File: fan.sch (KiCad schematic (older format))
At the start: 14 parts, among them J7 Fan In, J8 Fan Out, Q1 2N7002, Q2 2N7002, U9 TMP709

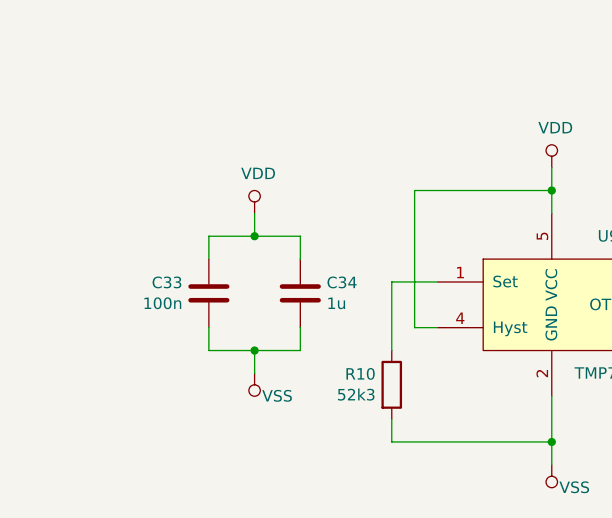
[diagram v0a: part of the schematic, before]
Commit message: Added optional through hole resistor to set fan switch on temperature.
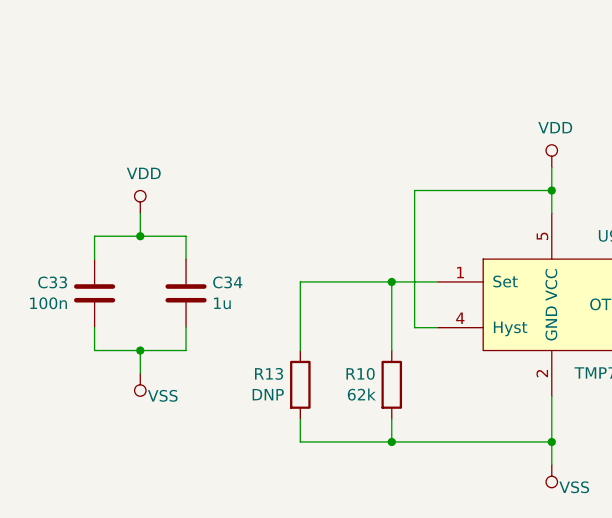
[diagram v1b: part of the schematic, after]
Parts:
- added R13: DNP, Resistor_THT:R_Axial_DIN0207_L6.3mm_D2.5mm_P10.16mm_Horizontal, symbol Device:R
- R10: value 52k3 -> 62k; lcsc# C218068 -> C351636; manf# ARG03FTC5232 -> PTFR0603B62K0P9
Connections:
- net VSS: now also R13.2
- net at R10.1, U9.1 (Set): now also R13.1
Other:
- moved on the sheet: C33, C34
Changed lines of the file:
@@
 AR Path="/5E453957/5E4A10E3" Ref="R10"  Part="1"
 F 0 "R10" H 2630 3896 50  0000 R CNN
-F 1 "52k3" H 2630 3805 50  0000 R CNN
+F 1 "62k" H 2630 3805 50  0000 R CNN
 F 2 "Resistor_SMD:R_0603_1608Metric" V 2630 3850 50  0001 C CNN
 F 3 "~" H 2700 3850 50  0001 C CNN
-F 4 "C218068" H 2700 3850 50  0001 C CNN "lcsc#"
-F 5 "ARG03FTC5232" H 2700 3850 50  0001 C CNN "manf#"
+F 4 "C351636" H 2700 3850 50  0001 C CNN "lcsc#"
+F 5 "PTFR0603B62K0P9" H 2700 3850 50  0001 C CNN "manf#"
 	1    2700 3850
 	1    0    0    -1
@@
 L Device:C C?
 U 1 1 5E4BEA5F
-P 1900 3450
+P 1400 3450
 AR Path="/5DD6D4DA/5DD6D50E/5E4BEA5F" Ref="C?"  Part="1"
 AR Path="/5DD6D4DA/5DDED058/5E4BEA5F" Ref="C?"  Part="1"
@@
 AR Path="/5E4BEA5F" Ref="C?"  Part="1"
 AR Path="/5E453957/5E4BEA5F" Ref="C33"  Part="1"
-F 0 "C33" H 2015 3496 50  0000 L CNN
-F 1 "100n" H 2015 3405 50  0000 L CNN
-F 2 "Capacitor_SMD:C_0603_1608Metric" H 1938 3300 50  0001 C CNN
-F 3 "~" H 1900 3450 50  0001 C CNN
-F 4 "CC0603KRX7R9BB104" H 1900 3450 50  0001 C CNN "manf#"
-F 5 "C14663" H 1900 3450 50  0001 C CNN "lcsc#"
-	1    1900 3450
+F 0 "C33" H 1515 3496 50  0000 L CNN
+F 1 "100n" H 1515 3405 50  0000 L CNN
+F 2 "Capacitor_SMD:C_0603_1608Metric" H 1438 3300 50  0001 C CNN
+F 3 "~" H 1400 3450 50  0001 C CNN
+F 4 "CC0603KRX7R9BB104" H 1400 3450 50  0001 C CNN "manf#"
+F 5 "C14663" H 1400 3450 50  0001 C CNN "lcsc#"
+	1    1400 3450
 	-1   0    0    -1
 $EndComp
@@
 L Device:C C?
 U 1 1 5E4BEA67
-P 2300 3450
+P 1800 3450
 AR Path="/5DD6D4DA/5DD6D50E/5E4BEA67" Ref="C?"  Part="1"
 AR Path="/5DD6D4DA/5DDED058/5E4BEA67" Ref="C?"  Part="1"
@@
 AR Path="/5E4BEA67" Ref="C?"  Part="1"
 AR Path="/5E453957/5E4BEA67" Ref="C34"  Part="1"
-F 0 "C34" H 2415 3496 50  0000 L CNN
-F 1 "1u" H 2415 3405 50  0000 L CNN
-F 2 "Capacitor_SMD:C_0805_2012Metric" H 2338 3300 50  0001 C CNN
-F 3 "~" H 2300 3450 50  0001 C CNN
-F 4 "CL21B105KBFNNNE" H 2300 3450 50  0001 C CNN "manf#"
-F 5 "C28323" H 2300 3450 50  0001 C CNN "lcsc#"
-	1    2300 3450
-	1    0    0    -1
-$EndComp
-Wire Wire Line
-	2100 3200 2100 3100
+F 0 "C34" H 1915 3496 50  0000 L CNN
+F 1 "1u" H 1915 3405 50  0000 L CNN
+F 2 "Capacitor_SMD:C_0805_2012Metric" H 1838 3300 50  0001 C CNN
+F 3 "~" H 1800 3450 50  0001 C CNN
+F 4 "CL21B105KBFNNNE" H 1800 3450 50  0001 C CNN "manf#"
+F 5 "C28323" H 1800 3450 50  0001 C CNN "lcsc#"
+	1    1800 3450
+	1    0    0    -1
+$EndComp
+Wire Wire Line
+	1600 3200 1600 3100
 $Comp
 L power:VDD #PWR?
 U 1 1 5E4C0B54
-P 2100 3100
+P 1600 3100
 AR Path="/5E3D0FD8/5E4C0B54" Ref="#PWR?"  Part="1"
 AR Path="/5E4C0B54" Ref="#PWR?"  Part="1"
 AR Path="/5E453957/5E4C0B54" Ref="#PWR044"  Part="1"
-F 0 "#PWR044" H 2100 2950 50  0001 C CNN
-F 1 "VDD" H 2117 3273 50  0000 C CNN
-F 2 "" H 2100 3100 50  0001 C CNN
-F 3 "" H 2100 3100 50  0001 C CNN
-	1    2100 3100
+F 0 "#PWR044" H 1600 2950 50  0001 C CNN
+F 1 "VDD" H 1617 3273 50  0000 C CNN
+F 2 "" H 1600 3100 50  0001 C CNN
+F 3 "" H 1600 3100 50  0001 C CNN
+	1    1600 3100
 	1    0    0    -1
 $EndComp
@@
 L power:VSS #PWR?
 U 1 1 5E4C1FB6
-P 2100 3800
+P 1600 3800
 AR Path="/5DD6D4DA/5DEBB035/5E4C1FB6" Ref="#PWR?"  Part="1"
 AR Path="/5E34CFA0/5E4C1FB6" Ref="#PWR?"  Part="1"
 AR Path="/5E3D0FD8/5E4C1FB6" Ref="#PWR?"  Part="1"
 AR Path="/5E453957/5E4C1FB6" Ref="#PWR045"  Part="1"
-F 0 "#PWR045" H 2100 3650 50  0001 C CNN
-F 1 "VSS" H 2000 3900 50  0000 C CNN
-F 2 "" H 2100 3800 50  0001 C CNN
-F 3 "" H 2100 3800 50  0001 C CNN
-	1    2100 3800
+F 0 "#PWR045" H 1600 3650 50  0001 C CNN
+F 1 "VSS" H 1500 3900 50  0000 C CNN
+F 2 "" H 1600 3800 50  0001 C CNN
+F 3 "" H 1600 3800 50  0001 C CNN
+	1    1600 3800
 	-1   0    0    1
 $EndComp
 Wire Wire Line
-	2100 3700 2100 3800
-Wire Wire Line
-	1900 3300 1900 3200
-Wire Wire Line
-	1900 3200 2100 3200
-Wire Wire Line
-	2300 3200 2300 3300
-Connection ~ 2100 3200
-Wire Wire Line
-	2100 3200 2300 3200
-Wire Wire Line
-	2300 3600 2300 3700
-Wire Wire Line
-	2300 3700 2100 3700
-Wire Wire Line
-	1900 3700 1900 3600
-Connection ~ 2100 3700
-Wire Wire Line
-	2100 3700 1900 3700
+	1600 3700 1600 3800
+Wire Wire Line
+	1400 3300 1400 3200
+Wire Wire Line
+	1400 3200 1600 3200
+Wire Wire Line
+	1800 3200 1800 3300
+Connection ~ 1600 3200
+Wire Wire Line
+	1600 3200 1800 3200
+Wire Wire Line
+	1800 3600 1800 3700
+Wire Wire Line
+	1800 3700 1600 3700
+Wire Wire Line
+	1400 3700 1400 3600
+Connection ~ 1600 3700
+Wire Wire Line
+	1600 3700 1400 3700
 $Comp
 L power:+VDC #PWR?
@@
 Wire Wire Line
 	6300 2100 6300 2400
+$Comp
+L Device:R R?
+U 1 1 5E617D39
+P 2300 3850
+AR Path="/5DD6D4DA/5DD6D50E/5E617D39" Ref="R?"  Part="1"
+AR Path="/5DD6D4DA/5DDED058/5E617D39" Ref="R?"  Part="1"
+AR Path="/5DD6D4DA/5DDED066/5E617D39" Ref="R?"  Part="1"
+AR Path="/5DD6D4DA/5DDED074/5E617D39" Ref="R?"  Part="1"
+AR Path="/5E46134B/5E617D39" Ref="R?"  Part="1"
+AR Path="/5E453957/5E617D39" Ref="R13"  Part="1"
+F 0 "R13" H 2230 3896 50  0000 R CNN
+F 1 "DNP" H 2230 3805 50  0000 R CNN
+F 2 "Resistor_THT:R_Axial_DIN0207_L6.3mm_D2.5mm_P10.16mm_Horizontal" V 2230 3850 50  0001 C CNN
+F 3 "~" H 2300 3850 50  0001 C CNN
+F 4 "DNP" H 2300 3850 50  0001 C CNN "DNP"
+	1    2300 3850
+	1    0    0    -1
+$EndComp
+Wire Wire Line
+	2300 4000 2300 4100
+Wire Wire Line
+	2300 4100 2700 4100
+Connection ~ 2700 4100
+Wire Wire Line
+	2300 3700 2300 3400
+Wire Wire Line
+	2300 3400 2700 3400
+Connection ~ 2700 3400
 $EndSCHEMATC
